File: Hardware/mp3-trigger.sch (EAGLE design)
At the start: 88 parts, among them IC1 LM1117, J1 POWER_JACKTOE, Q1 12.288MHz, U1 CY8C29466, U10 M18_, U2 USD-SOCKET, U3 MUX-74HC4067SMD, U5 1.8V Reg, U6 NAV_SWITCHSMD, U7 VS1063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

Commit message: Minor changes from Toni K review
Acid trap elimination, angles, added notes about jumpers, minor
rerouting.
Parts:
- removed FRAME1: FRAME-LETTERNO_PACKAGE, SparkFun-Aesthetics:FRAME-LETTERNO_PACKAGE
- removed U$3: LOGO-SFESK, SparkFun:LOGO-SFESK
- added LOGO1: SFE_LOGO_FLAME.3_INCH, SparkFun-Aesthetics:SFE_LOGO_FLAME.3_INCH
- added U$4: REVISION, SparkFun-Aesthetics:REVISION
- JP6, JP7: device SparkFun:FIDUCIAL1X2 -> SparkFun-Aesthetics:FIDUCIAL1X2
- U$1: value LOGO-SFENEW -> SFE_LOGO_NAME_FLAME.2_INCH; device SparkFun:LOGO-SFENEW -> SparkFun-Aesthetics:SFE_LOGO_NAME_FLAME.2_INCH
- U$12, U$13, U$14, U$15: device SparkFun:STAND-OFF -> SparkFun-Electromechanical:STAND-OFF
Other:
- note added: "By default, SJ1 is set to power the board through the barrel jack at 4.5-12V. To power with a 3.3V regulated source through the FTDI header, set the jumper to the alternate configuration."
- note added: "Each of these audio jumpers adds proper ac coupling to the audio output that will prevent problems when connecting to audio equipment. To revert back to the original audio design before V24, solder all three jumpers to the opposite configuration."
- note added: "Joel Bartlett"
- note added: "Revision by: Joel Bartlett"
- note removed: "Updated by: Joel Bartlett"
- moved on the sheet: C1, C10, C11, C15, C16, C6, C9, JP2, LED2, Q1, R13, R14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

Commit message: Added OSHW Logo
Added OSHW Logo
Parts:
- added LOGO3: OSHW-LOGOM, SparkFun-Aesthetics:OSHW-LOGOM
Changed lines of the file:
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@@
 <part name="U$4" library="SparkFun-Aesthetics" deviceset="REVISION" device=""/>
 <part name="LOGO1" library="SparkFun-Aesthetics" deviceset="SFE_LOGO_FLAME" device=".3_INCH"/>
+<part name="LOGO3" library="SparkFun-Aesthetics" deviceset="OSHW-LOGO" device="M"/>
 </parts>
 <sheets>
@@
 <instance part="R12" gate="G$1" x="215.9" y="81.28" rot="R90"/>
 <instance part="P+11" gate="G$1" x="215.9" y="88.9"/>
+<instance part="LOGO3" gate="G$1" x="180.34" y="45.72"/>
 </instances>
 <busses>

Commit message: QC Checklist Crrections
Minor error fixes
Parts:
- added FRAME1: FRAME-LETTERNO_PACKAGE, SparkFun-Aesthetics:FRAME-LETTERNO_PACKAGE
- renumbered IC1 to U4

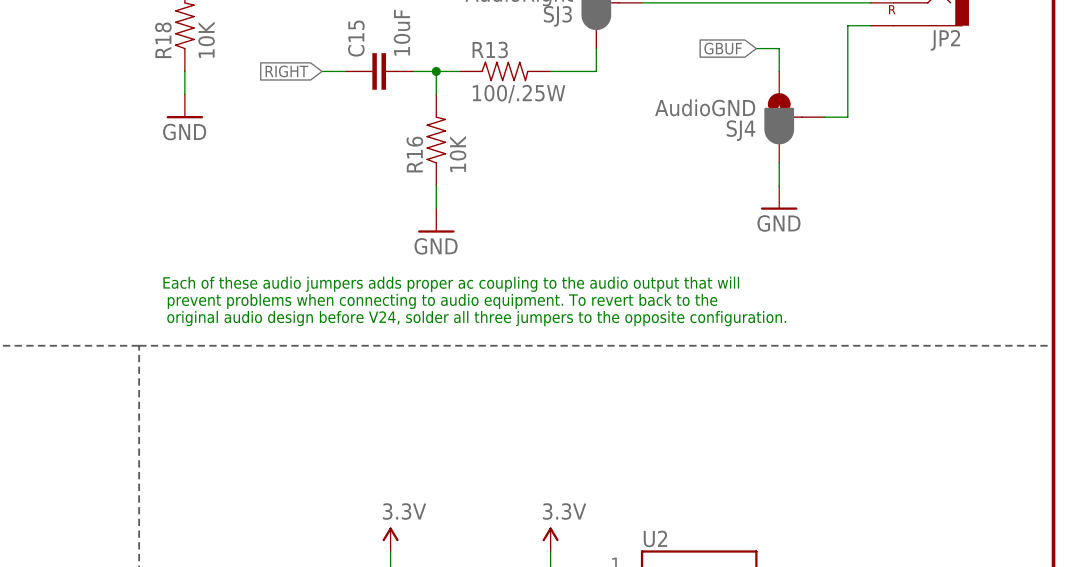
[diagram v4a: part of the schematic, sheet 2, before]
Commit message: FTDI Silk update
Changed to 5V FTDI
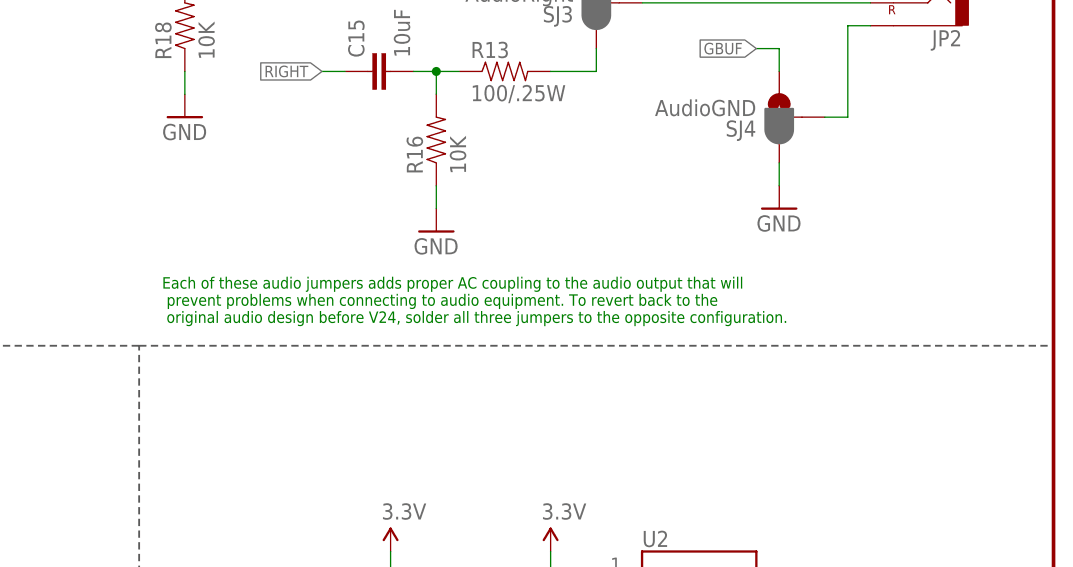
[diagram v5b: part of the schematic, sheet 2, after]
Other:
- note added: "Each of these audio jumpers adds proper AC coupling to the audio output that will prevent problems when connecting to audio equipment. To revert back to the original audio design before V24, solder all three jumpers to the opposite configuration."
- note removed: "Each of these audio jumpers adds proper ac coupling to the audio output that will prevent problems when connecting to audio equipment. To revert back to the original audio design before V24, solder all three jumpers to the opposite configuration."
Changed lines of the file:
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@@
 <?xml version="1.0" encoding="utf-8"?>
 <!DOCTYPE eagle SYSTEM "eagle.dtd">
-<eagle version="7.2.0">
+<eagle version="7.3.0">
 <drawing>
 <settings>
@@
 <grid distance="0.1" unitdist="inch" unit="inch" style="lines" multiple="1" display="no" altdistance="0.01" altunitdist="inch" altunit="inch"/>
 <layers>
-<layer number="1" name="Top" color="4" fill="1" visible="yes" active="no"/>
-<layer number="2" name="Route2" color="1" fill="3" visible="yes" active="no"/>
-<layer number="3" name="Route3" color="4" fill="3" visible="yes" active="no"/>
-<layer number="4" name="Route4" color="1" fill="4" visible="yes" active="no"/>
-<layer number="5" name="Route5" color="4" fill="4" visible="yes" active="no"/>
-<layer number="6" name="Route6" color="1" fill="8" visible="yes" active="no"/>
-<layer number="7" name="Route7" color="4" fill="8" visible="yes" active="no"/>
-<layer number="8" name="Route8" color="1" fill="2" visible="yes" active="no"/>
-<layer number="9" name="Route9" color="4" fill="2" visible="yes" active="no"/>
-<layer number="10" name="Route10" color="1" fill="7" visible="yes" active="no"/>
-<layer number="11" name="Route11" color="4" fill="7" visible="yes" active="no"/>
-<layer number="12" name="Route12" color="1" fill="5" visible="yes" active="no"/>
-<layer number="13" name="Route13" color="4" fill="5" visible="yes" active="no"/>
-<layer number="14" name="Route14" color="1" fill="6" visible="yes" active="no"/>
-<layer number="15" name="Route15" color="4" fill="6" visible="yes" active="no"/>
-<layer number="16" name="Bottom" color="1" fill="1" visible="yes" active="no"/>
-<layer number="17" name="Pads" color="2" fill="1" visible="yes" active="no"/>
-<layer number="18" name="Vias" color="2" fill="1" visible="yes" active="no"/>
-<layer number="19" name="Unrouted" color="6" fill="1" visible="yes" active="no"/>
-<layer number="20" name="Dimension" color="15" fill="1" visible="yes" active="no"/>
-<layer number="21" name="tPlace" color="16" fill="1" visible="yes" active="no"/>
-<layer number="22" name="bPlace" color="14" fill="1" visible="yes" active="no"/>
-<layer number="23" name="tOrigins" color="15" fill="1" visible="yes" active="no"/>
-<layer number="24" name="bOrigins" color="15" fill="1" visible="yes" active="no"/>
-<layer number="25" name="tNames" color="7" fill="1" visible="yes" active="no"/>
-<layer number="26" name="bNames" color="7" fill="1" visible="yes" active="no"/>
-<layer number="27" name="tValues" color="7" fill="1" visible="yes" active="no"/>
-<layer number="28" name="bValues" color="7" fill="1" visible="yes" active="no"/>
+<layer number="1" name="Top" color="4" fill="1" visible="no" active="no"/>
+<layer number="2" name="Route2" color="1" fill="3" visible="no" active="no"/>
+<layer number="3" name="Route3" color="4" fill="3" visible="no" active="no"/>
+<layer number="4" name="Route4" color="1" fill="4" visible="no" active="no"/>
+<layer number="5" name="Route5" color="4" fill="4" visible="no" active="no"/>
+<layer number="6" name="Route6" color="1" fill="8" visible="no" active="no"/>
+<layer number="7" name="Route7" color="4" fill="8" visible="no" active="no"/>
+<layer number="8" name="Route8" color="1" fill="2" visible="no" active="no"/>
+<layer number="9" name="Route9" color="4" fill="2" visible="no" active="no"/>
+<layer number="10" name="Route10" color="1" fill="7" visible="no" active="no"/>
+<layer number="11" name="Route11" color="4" fill="7" visible="no" active="no"/>
+<layer number="12" name="Route12" color="1" fill="5" visible="no" active="no"/>
+<layer number="13" name="Route13" color="4" fill="5" visible="no" active="no"/>
+<layer number="14" name="Route14" color="1" fill="6" visible="no" active="no"/>
+<layer number="15" name="Route15" color="4" fill="6" visible="no" active="no"/>
+<layer number="16" name="Bottom" color="1" fill="1" visible="no" active="no"/>
+<layer number="17" name="Pads" color="2" fill="1" visible="no" active="no"/>
+<layer number="18" name="Vias" color="2" fill="1" visible="no" active="no"/>
+<layer number="19" name="Unrouted" color="6" fill="1" visible="no" active="no"/>
+<layer number="20" name="Dimension" color="15" fill="1" visible="no" active="no"/>
+<layer number="21" name="tPlace" color="16" fill="1" visible="no" active="no"/>
+<layer number="22" name="bPlace" color="14" fill="1" visible="no" active="no"/>
+<layer number="23" name="tOrigins" color="15" fill="1" visible="no" active="no"/>
+<layer number="24" name="bOrigins" color="15" fill="1" visible="no" active="no"/>
+<layer number="25" name="tNames" color="7" fill="1" visible="no" active="no"/>
+<layer number="26" name="bNames" color="7" fill="1" visible="no" active="no"/>
+<layer number="27" name="tValues" color="7" fill="1" visible="no" active="no"/>
+<layer number="28" name="bValues" color="7" fill="1" visible="no" active="no"/>
 <layer number="29" name="tStop" color="7" fill="3" visible="no" active="no"/>
 <layer number="30" name="bStop" color="7" fill="6" visible="no" active="no"/>
@@
 <layer number="35" name="tGlue" color="7" fill="4" visible="no" active="no"/>
 <layer number="36" name="bGlue" color="7" fill="5" visible="no" active="no"/>
-<layer number="37" name="tTest" color="7" fill="1" visible="yes" active="no"/>
-<layer number="38" name="bTest" color="7" fill="1" visible="yes" active="no"/>
+<layer number="37" name="tTest" color="7" fill="1" visible="no" active="no"/>
+<layer number="38" name="bTest" color="7" fill="1" visible="no" active="no"/>
 <layer number="39" name="tKeepout" color="4" fill="11" visible="no" active="no"/>
 <layer number="40" name="bKeepout" color="1" fill="11" visible="no" active="no"/>
@@
 <layer number="44" name="Drills" color="7" fill="1" visible="no" active="no"/>
 <layer number="45" name="Holes" color="7" fill="1" visible="no" active="no"/>
-<layer number="46" name="Milling" color="3" fill="1" visible="yes" active="no"/>
-<layer number="47" name="Measures" color="7" fill="1" visible="yes" active="no"/>
-<layer number="48" name="Document" color="7" fill="1" visible="yes" active="no"/>
-<layer number="49" name="Reference" color="7" fill="1" visible="yes" active="no"/>
-<layer number="50" name="dxf" color="7" fill="1" visible="yes" active="no"/>
-<layer number="51" name="tDocu" color="6" fill="1" visible="yes" active="no"/>
-<layer number="52" name="bDocu" color="7" fill="1" visible="yes" active="no"/>
-<layer number="53" name="tGND_GNDA" color="7" fill="9" visible="yes" active="no"/>
-<layer number="54" name="bGND_GNDA" color="1" fill="9" visible="yes" active="no"/>
-<layer number="56" name="wert" color="7" fill="1" visible="yes" active="no"/>
-<layer number="57" name="tCAD" color="7" fill="1" visible="yes" active="no"/>
-<layer number="59" name="tCarbon" color="7" fill="1" visible="yes" active="no"/>
-<layer number="60" name="bCarbon" color="7" fill="1" visible="yes" active="no"/>
+<layer number="46" name="Milling" color="3" fill="1" visible="no" active="no"/>
+<layer number="47" name="Measures" color="7" fill="1" visible="no" active="no"/>
+<layer number="48" name="Document" color="7" fill="1" visible="no" active="no"/>
+<layer number="49" name="Reference" color="7" fill="1" visible="no" active="no"/>
+<layer number="50" name="dxf" color="7" fill="1" visible="no" active="no"/>
+<layer number="51" name="tDocu" color="6" fill="1" visible="no" active="no"/>
+<layer number="52" name="bDocu" color="7" fill="1" visible="no" active="no"/>
+<layer number="53" name="tGND_GNDA" color="7" fill="9" visible="no" active="no"/>
+<layer number="54" name="bGND_GNDA" color="1" fill="9" visible="no" active="no"/>
+<layer number="56" name="wert" color="7" fill="1" visible="no" active="no"/>
+<layer number="57" name="tCAD" color="7" fill="1" visible="no" active="no"/>
+<layer number="59" name="tCarbon" color="7" fill="1" visible="no" active="no"/>
+<layer number="60" name="bCarbon" color="7" fill="1" visible="no" active="no"/>
 <layer number="90" name="Modules" color="5" fill="1" visible="yes" active="yes"/>
 <layer number="91" name="Nets" color="2" fill="1" visible="yes" active="yes"/>
@@
 <text x="139.7" y="180.34" size="2.54" layer="94" font="vector">Audio</text>
 <text x="25.4" y="177.8" size="2.54" layer="94" font="vector">1.8V Regulator</text>
-<text x="149.86" y="124.46" size="1.27" layer="91" font="vector">Each of these audio jumpers adds proper ac coupling to the audio output that will
+<text x="149.86" y="124.46" size="1.27" layer="91" font="vector">Each of these audio jumpers adds proper AC coupling to the audio output that will
  prevent problems when connecting to audio equipment. To revert back to the
  original audio design before V24, solder all three jumpers to the opposite configuration. </text>
